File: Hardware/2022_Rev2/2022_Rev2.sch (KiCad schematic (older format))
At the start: 35 parts

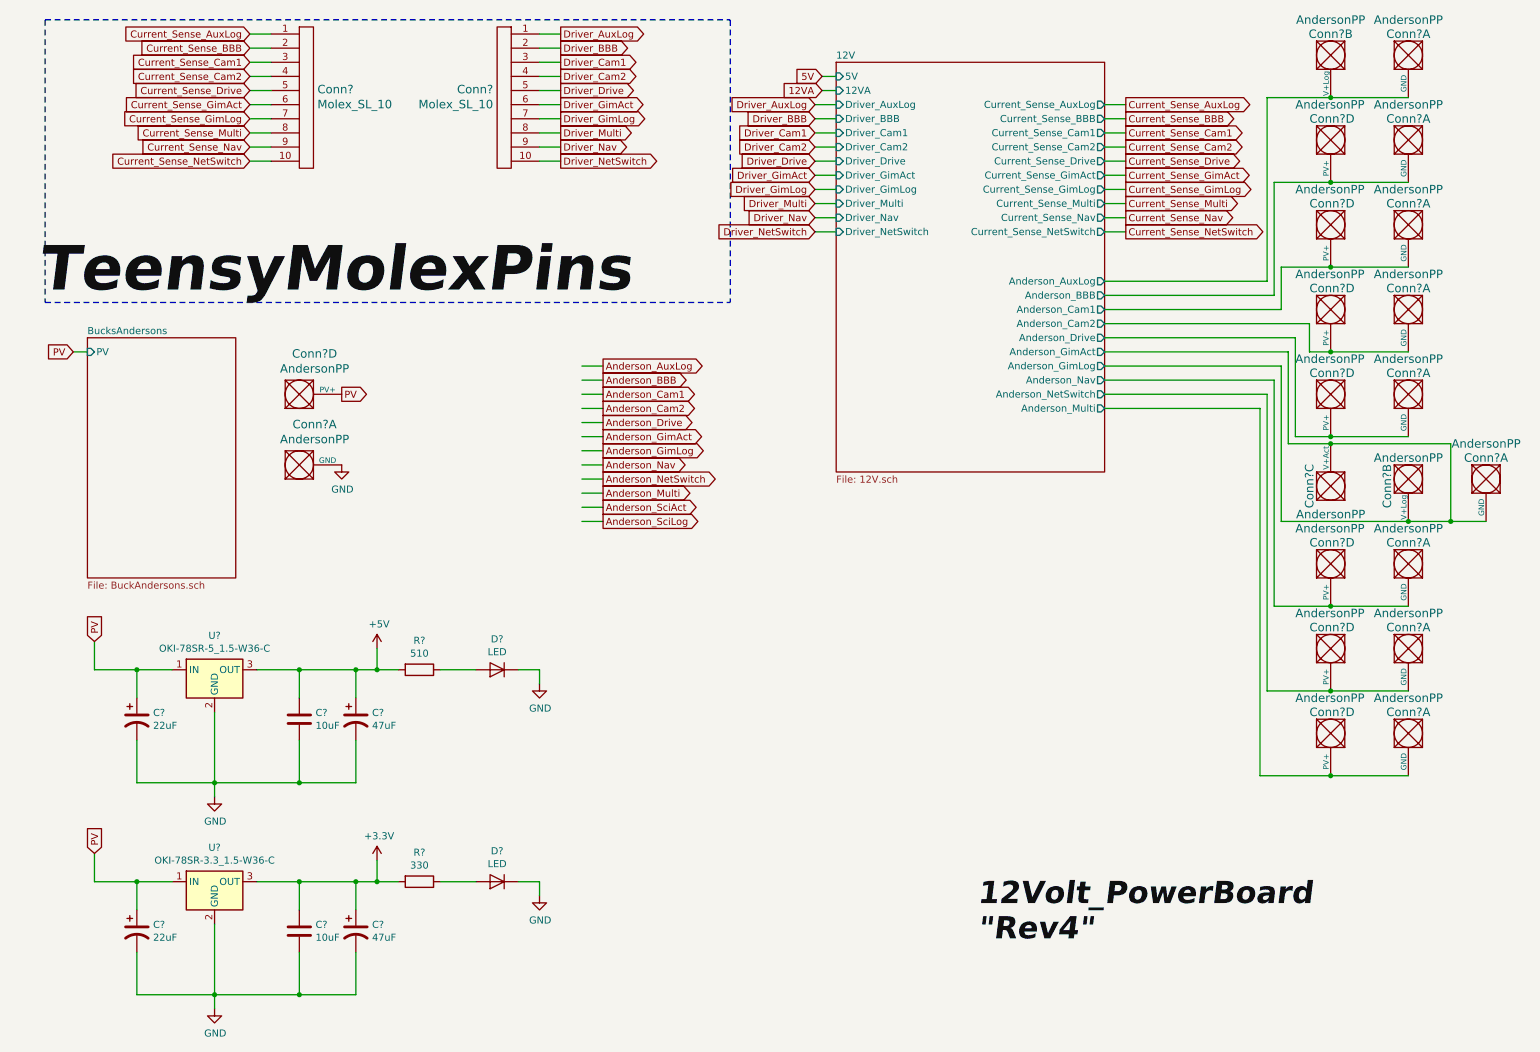
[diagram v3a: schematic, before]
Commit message: assigning footprints pt.1
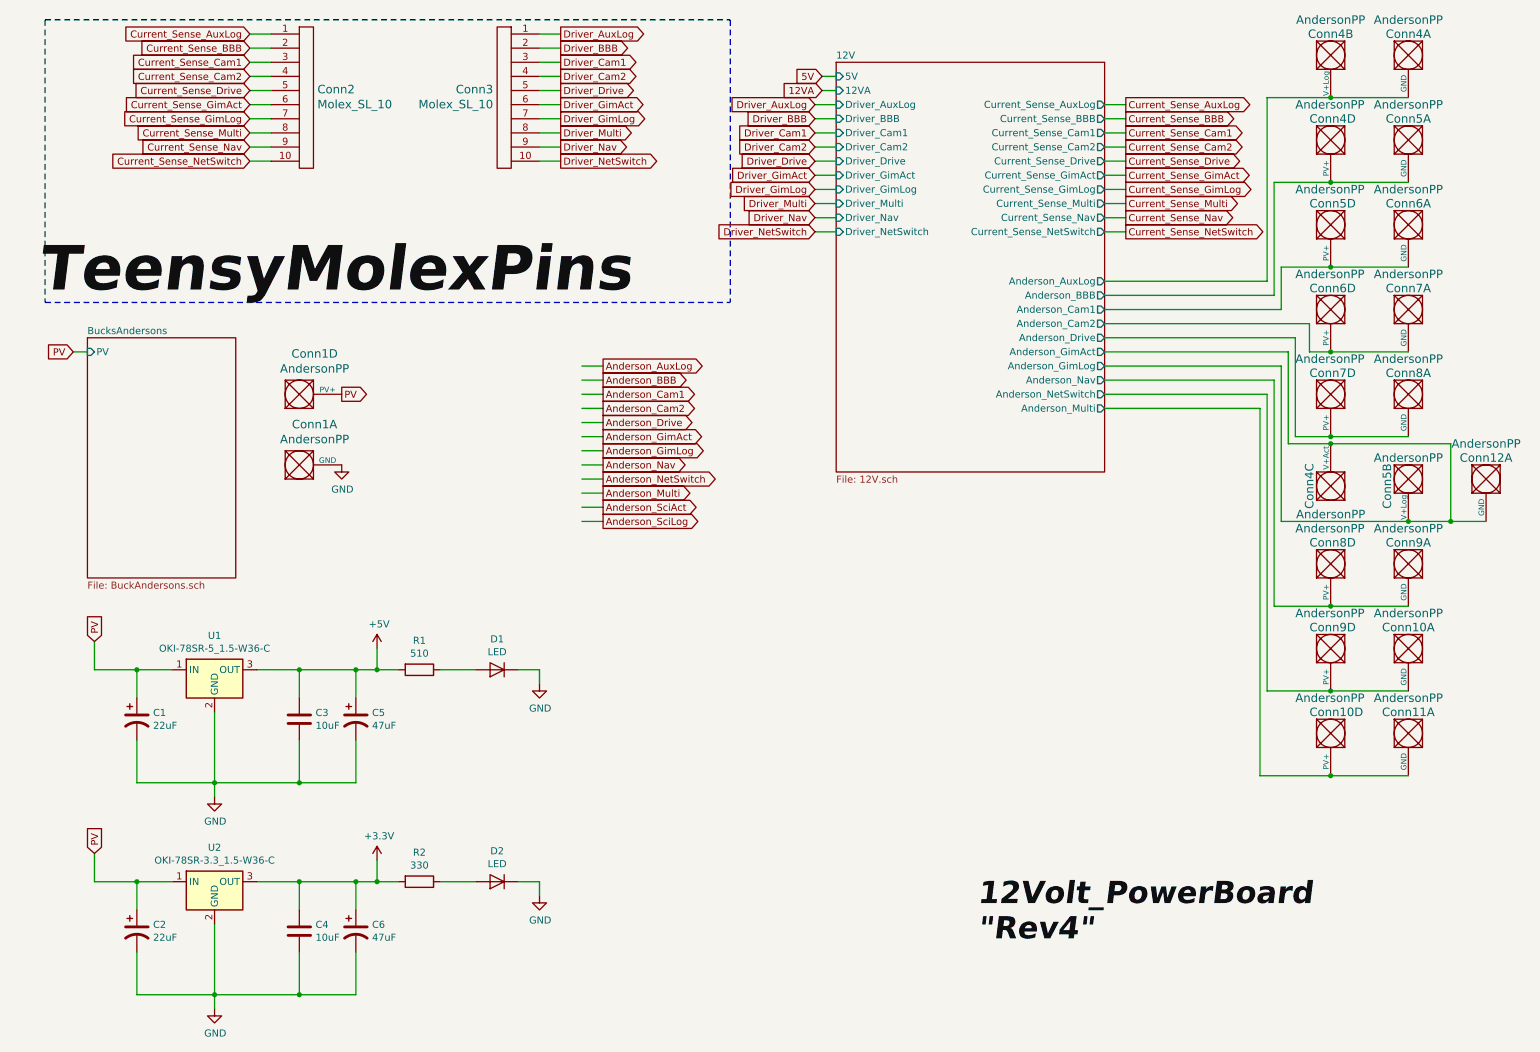
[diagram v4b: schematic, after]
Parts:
- C1, C2, C5, C6: renamed from C?; footprint (none) -> Capacitor_THT:CP_Radial_D6.3mm_P2.50mm
- C3, C4: renamed from C?; footprint (none) -> Capacitor_SMD:C_0603_1608Metric_Pad1.08x0.95mm_HandSolder
- D1, D2: renamed from D?; footprint (none) -> Diode_SMD:D_0603_1608Metric_Pad1.05x0.95mm_HandSolder
- gave numbers to parts that had none: 16

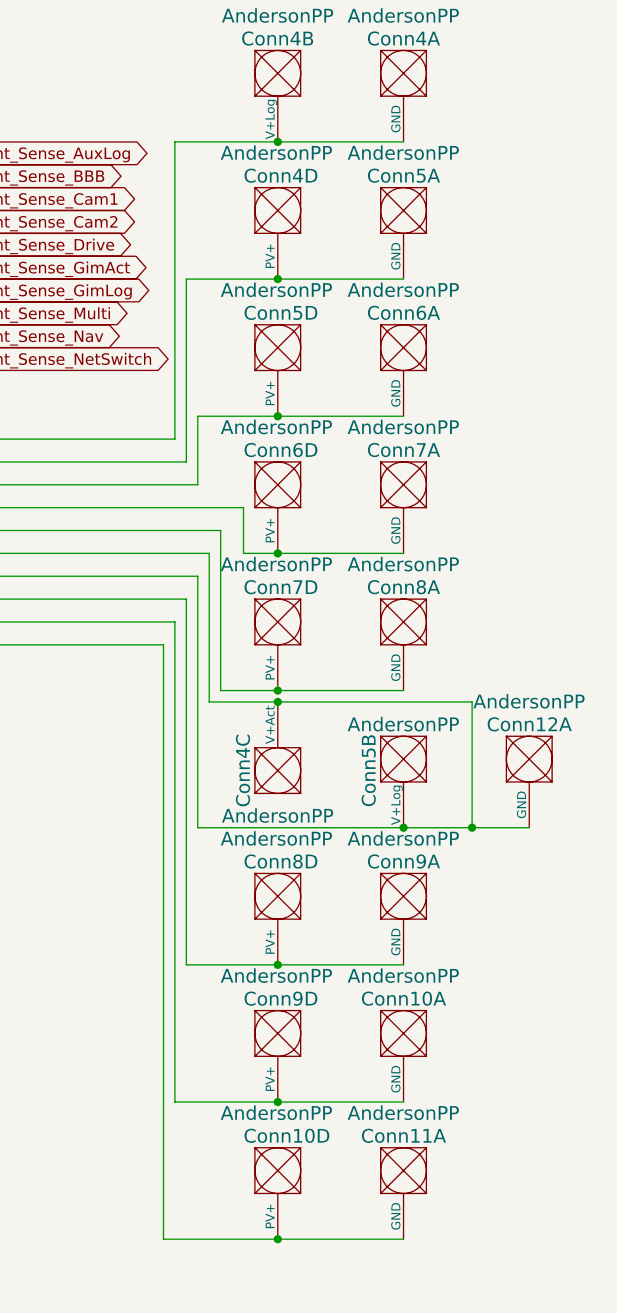
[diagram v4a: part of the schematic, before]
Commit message: Finished footprint signatures and started schematic
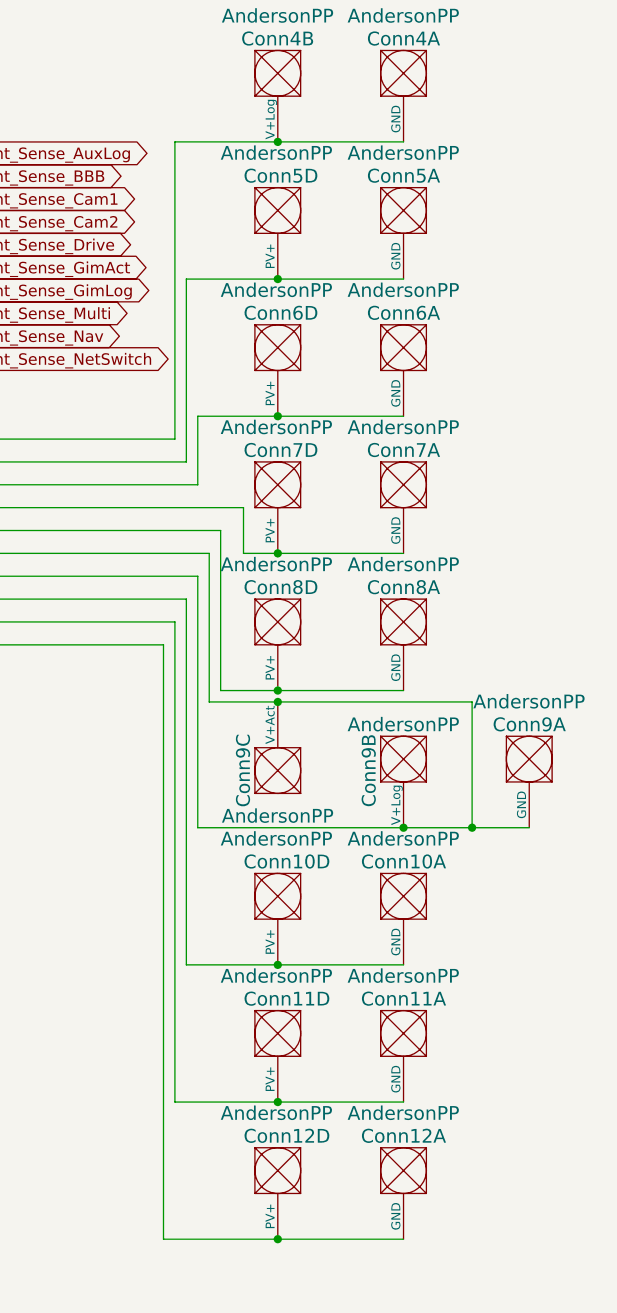
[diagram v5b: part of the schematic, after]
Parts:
- Conn1: footprint (none) -> MRDT_Connectors:Anderson_2_Vertical_Side_by_Side_PV
- Conn10, Conn11: renamed from Conn9; footprint (none) -> MRDT_Connectors:Anderson_2_Horizontal_Side_by_Side_PV
- Conn10: renamed from Conn8; footprint (none) -> MRDT_Connectors:Anderson_2_Horizontal_Side_by_Side_PV
- Conn11, Conn12: renamed from Conn10; footprint (none) -> MRDT_Connectors:Anderson_2_Horizontal_Side_by_Side_PV
- Conn12: renamed from Conn11; footprint (none) -> MRDT_Connectors:Anderson_2_Horizontal_Side_by_Side_PV
- Conn2, Conn3: footprint (none) -> MRDT_Connectors:MOLEX_SL_10_Vertical
- Conn4, Conn5, Conn6, Conn7, Conn8: footprint (none) -> MRDT_Connectors:Anderson_2_Horizontal_Side_by_Side_PV
- Conn5: renamed from Conn4; footprint (none) -> MRDT_Connectors:Anderson_2_Horizontal_Side_by_Side_PV
- Conn6: renamed from Conn5; footprint (none) -> MRDT_Connectors:Anderson_2_Horizontal_Side_by_Side_PV
- Conn7: renamed from Conn6; footprint (none) -> MRDT_Connectors:Anderson_2_Horizontal_Side_by_Side_PV
- Conn8: renamed from Conn7; footprint (none) -> MRDT_Connectors:Anderson_2_Horizontal_Side_by_Side_PV
- Conn9: renamed from Conn4; footprint (none) -> MRDT_Connectors:Anderson_3_Horizontal_Side_by_Side
- Conn9: renamed from Conn5; footprint (none) -> MRDT_Connectors:Anderson_3_Horizontal_Side_by_Side
- Conn9: renamed from Conn12; footprint (none) -> MRDT_Connectors:Anderson_3_Horizontal_Side_by_Side
- R1, R2: footprint (none) -> Resistor_SMD:R_0603_1608Metric_Pad0.98x0.95mm_HandSolder
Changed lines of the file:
@@
 F 0 "Conn1" H 2408 3637 60  0000 C CNN
 F 1 "AndersonPP" H 2408 3531 60  0000 C CNN
-F 2 "" H 2050 2700 60  0001 C CNN
+F 2 "MRDT_Connectors:Anderson_2_Vertical_Side_by_Side_PV" H 2050 2700 60  0001 C CNN
 F 3 "" H 2050 2700 60  0001 C CNN
 	4    2200 3250
@@
 F 0 "Conn1" H 2408 4137 60  0000 C CNN
 F 1 "AndersonPP" H 2408 4031 60  0000 C CNN
-F 2 "" H 2050 3200 60  0001 C CNN
+F 2 "MRDT_Connectors:Anderson_2_Vertical_Side_by_Side_PV" H 2050 3200 60  0001 C CNN
 F 3 "" H 2050 3200 60  0001 C CNN
 	1    2200 3750
@@
 F 0 "R1" V 2943 5100 50  0000 C CNN
 F 1 "510" V 3034 5100 50  0000 C CNN
-F 2 "" V 3080 5100 50  0001 C CNN
+F 2 "Resistor_SMD:R_0603_1608Metric_Pad0.98x0.95mm_HandSolder" V 3080 5100 50  0001 C CNN
 F 3 "~" H 3150 5100 50  0001 C CNN
 	1    3150 5100
@@
 F 0 "R2" V 2943 6600 50  0000 C CNN
 F 1 "330" V 3034 6600 50  0000 C CNN
-F 2 "" V 3080 6600 50  0001 C CNN
+F 2 "Resistor_SMD:R_0603_1608Metric_Pad0.98x0.95mm_HandSolder" V 3080 6600 50  0001 C CNN
 F 3 "~" H 3150 6600 50  0001 C CNN
 	1    3150 6600
@@
 F 0 "Conn4" V 9450 750 60  0000 C CNN
 F 1 "AndersonPP" V 9350 750 60  0000 C CNN
-F 2 "" H 9350 100 60  0001 C CNN
+F 2 "MRDT_Connectors:Anderson_2_Horizontal_Side_by_Side_PV" H 9350 100 60  0001 C CNN
 F 3 "" H 9350 100 60  0001 C CNN
 	2    9500 650
@@
 $EndComp
 $Comp
-L MRDT_Connectors:AndersonPP Conn12
+L MRDT_Connectors:AndersonPP Conn9
 U 1 1 62580F86
 P 10600 3650
-F 0 "Conn12" V 10550 3750 60  0000 C CNN
+F 0 "Conn9" V 10550 3750 60  0000 C CNN
 F 1 "AndersonPP" V 10450 3750 60  0000 C CNN
-F 2 "" H 10450 3100 60  0001 C CNN
+F 2 "MRDT_Connectors:Anderson_3_Horizontal_Side_by_Side" H 10450 3100 60  0001 C CNN
 F 3 "" H 10450 3100 60  0001 C CNN
 	1    10600 3650
@@
 F 0 "Conn4" V 10000 750 60  0000 C CNN
 F 1 "AndersonPP" V 9900 750 60  0000 C CNN
-F 2 "" H 9900 100 60  0001 C CNN
+F 2 "MRDT_Connectors:Anderson_2_Horizontal_Side_by_Side_PV" H 9900 100 60  0001 C CNN
 F 3 "" H 9900 100 60  0001 C CNN
 	1    10050 650
@@
 F 0 "Conn5" V 10000 1350 60  0000 C CNN
 F 1 "AndersonPP" V 9900 1350 60  0000 C CNN
-F 2 "" H 9900 700 60  0001 C CNN
+F 2 "MRDT_Connectors:Anderson_2_Horizontal_Side_by_Side_PV" H 9900 700 60  0001 C CNN
 F 3 "" H 9900 700 60  0001 C CNN
 	1    10050 1250
@@
 F 0 "Conn6" V 10000 1950 60  0000 C CNN
 F 1 "AndersonPP" V 9900 1950 60  0000 C CNN
-F 2 "" H 9900 1300 60  0001 C CNN
+F 2 "MRDT_Connectors:Anderson_2_Horizontal_Side_by_Side_PV" H 9900 1300 60  0001 C CNN
 F 3 "" H 9900 1300 60  0001 C CNN
 	1    10050 1850
@@
 F 0 "Conn7" V 10000 2550 60  0000 C CNN
 F 1 "AndersonPP" V 9900 2550 60  0000 C CNN
-F 2 "" H 9900 1900 60  0001 C CNN
+F 2 "MRDT_Connectors:Anderson_2_Horizontal_Side_by_Side_PV" H 9900 1900 60  0001 C CNN
 F 3 "" H 9900 1900 60  0001 C CNN
 	1    10050 2450
@@
 $EndComp
 $Comp
-L MRDT_Connectors:AndersonPP Conn4
+L MRDT_Connectors:AndersonPP Conn9
 U 3 1 6257FC90
 P 9700 3900
-F 0 "Conn4" H 9800 4150 60  0000 C CNN
+F 0 "Conn9" H 9800 4150 60  0000 C CNN
 F 1 "AndersonPP" V 9600 4000 60  0000 C CNN
-F 2 "" H 9550 3350 60  0001 C CNN
+F 2 "MRDT_Connectors:Anderson_3_Horizontal_Side_by_Side" H 9550 3350 60  0001 C CNN
 F 3 "" H 9550 3350 60  0001 C CNN
 	3    9700 3900
@@
 $EndComp
 $Comp
-L MRDT_Connectors:AndersonPP Conn9
+L MRDT_Connectors:AndersonPP Conn10
 U 1 1 625DF808
 P 10050 4250
-F 0 "Conn9" V 10000 4350 60  0000 C CNN
+F 0 "Conn10" V 10000 4350 60  0000 C CNN
 F 1 "AndersonPP" V 9900 4350 60  0000 C CNN
-F 2 "" H 9900 3700 60  0001 C CNN
+F 2 "MRDT_Connectors:Anderson_2_Horizontal_Side_by_Side_PV" H 9900 3700 60  0001 C CNN
 F 3 "" H 9900 3700 60  0001 C CNN
 	1    10050 4250
@@
 $EndComp
 $Comp
-L MRDT_Connectors:AndersonPP Conn10
+L MRDT_Connectors:AndersonPP Conn11
 U 1 1 625E3A96
 P 10050 4850
-F 0 "Conn10" V 10000 4950 60  0000 C CNN
+F 0 "Conn11" V 10000 4950 60  0000 C CNN
 F 1 "AndersonPP" V 9900 4950 60  0000 C CNN
-F 2 "" H 9900 4300 60  0001 C CNN
+F 2 "MRDT_Connectors:Anderson_2_Horizontal_Side_by_Side_PV" H 9900 4300 60  0001 C CNN
 F 3 "" H 9900 4300 60  0001 C CNN
 	1    10050 4850
@@
 $EndComp
 $Comp
-L MRDT_Connectors:AndersonPP Conn11
+L MRDT_Connectors:AndersonPP Conn12
 U 1 1 625EBE27
 P 10050 5450
-F 0 "Conn11" V 10000 5550 60  0000 C CNN
+F 0 "Conn12" V 10000 5550 60  0000 C CNN
 F 1 "AndersonPP" V 9900 5550 60  0000 C CNN
-F 2 "" H 9900 4900 60  0001 C CNN
+F 2 "MRDT_Connectors:Anderson_2_Horizontal_Side_by_Side_PV" H 9900 4900 60  0001 C CNN
 F 3 "" H 9900 4900 60  0001 C CNN
 	1    10050 5450
@@
 	9450 2650 9450 2850
 $Comp
-L MRDT_Connectors:AndersonPP Conn4
+L MRDT_Connectors:AndersonPP Conn5
 U 4 1 6265DE23
 P 9500 1250
-F 0 "Conn4" V 9450 1200 60  0000 L CNN
+F 0 "Conn5" V 9450 1200 60  0000 L CNN
 F 1 "AndersonPP" V 9350 1100 60  0000 L CNN
-F 2 "" H 9350 700 60  0001 C CNN
+F 2 "MRDT_Connectors:Anderson_2_Horizontal_Side_by_Side_PV" H 9350 700 60  0001 C CNN
 F 3 "" H 9350 700 60  0001 C CNN
 	4    9500 1250
@@
 	9600 1650 10150 1650
 $Comp
-L MRDT_Connectors:AndersonPP Conn5
+L MRDT_Connectors:AndersonPP Conn6
 U 4 1 62664C16
 P 9500 1850
-F 0 "Conn5" V 9450 1800 60  0000 L CNN
+F 0 "Conn6" V 9450 1800 60  0000 L CNN
 F 1 "AndersonPP" V 9350 1700 60  0000 L CNN
-F 2 "" H 9350 1300 60  0001 C CNN
+F 2 "MRDT_Connectors:Anderson_2_Horizontal_Side_by_Side_PV" H 9350 1300 60  0001 C CNN
 F 3 "" H 9350 1300 60  0001 C CNN
 	4    9500 1850
@@
 $EndComp
 $Comp
-L MRDT_Connectors:AndersonPP Conn6
+L MRDT_Connectors:AndersonPP Conn7
 U 4 1 62669E3D
 P 9500 2450
-F 0 "Conn6" V 9450 2400 60  0000 L CNN
+F 0 "Conn7" V 9450 2400 60  0000 L CNN
 F 1 "AndersonPP" V 9350 2300 60  0000 L CNN
-F 2 "" H 9350 1900 60  0001 C CNN
+F 2 "MRDT_Connectors:Anderson_2_Horizontal_Side_by_Side_PV" H 9350 1900 60  0001 C CNN
 F 3 "" H 9350 1900 60  0001 C CNN
 	4    9500 2450
@@
 $EndComp
 $Comp
-L MRDT_Connectors:AndersonPP Conn7
+L MRDT_Connectors:AndersonPP Conn8
 U 4 1 62679AA7
 P 9500 3050
-F 0 "Conn7" V 9450 3000 60  0000 L CNN
+F 0 "Conn8" V 9450 3000 60  0000 L CNN
 F 1 "AndersonPP" V 9350 2900 60  0000 L CNN
-F 2 "" H 9350 2500 60  0001 C CNN
+F 2 "MRDT_Connectors:Anderson_2_Horizontal_Side_by_Side_PV" H 9350 2500 60  0001 C CNN
 F 3 "" H 9350 2500 60  0001 C CNN
 	4    9500 3050
@@
 F 0 "Conn8" V 10000 3150 60  0000 C CNN
 F 1 "AndersonPP" V 9900 3150 60  0000 C CNN
-F 2 "" H 9900 2500 60  0001 C CNN
+F 2 "MRDT_Connectors:Anderson_2_Horizontal_Side_by_Side_PV" H 9900 2500 60  0001 C CNN
 F 3 "" H 9900 2500 60  0001 C CNN
 	1    10050 3050
@@
 	9600 2250 10150 2250
 $Comp
-L MRDT_Connectors:AndersonPP Conn8
+L MRDT_Connectors:AndersonPP Conn10
 U 4 1 62690D22
 P 9500 4250
-F 0 "Conn8" V 9450 4200 60  0000 L CNN
+F 0 "Conn10" V 9450 4200 60  0000 L CNN
 F 1 "AndersonPP" V 9350 4100 60  0000 L CNN
-F 2 "" H 9350 3700 60  0001 C CNN
+F 2 "MRDT_Connectors:Anderson_2_Horizontal_Side_by_Side_PV" H 9350 3700 60  0001 C CNN
 F 3 "" H 9350 3700 60  0001 C CNN
 	4    9500 4250
@@
 $EndComp
 $Comp
-L MRDT_Connectors:AndersonPP Conn9
+L MRDT_Connectors:AndersonPP Conn11
 U 4 1 626957E9
 P 9500 4850
-F 0 "Conn9" V 9450 4800 60  0000 L CNN
+F 0 "Conn11" V 9450 4800 60  0000 L CNN
 F 1 "AndersonPP" V 9350 4700 60  0000 L CNN
-F 2 "" H 9350 4300 60  0001 C CNN
+F 2 "MRDT_Connectors:Anderson_2_Horizontal_Side_by_Side_PV" H 9350 4300 60  0001 C CNN
 F 3 "" H 9350 4300 60  0001 C CNN
 	4    9500 4850
@@
 $EndComp
 $Comp
-L MRDT_Connectors:AndersonPP Conn10
+L MRDT_Connectors:AndersonPP Conn12
 U 4 1 6269A40C
 P 9500 5450
-F 0 "Conn10" V 9450 5400 60  0000 L CNN
+F 0 "Conn12" V 9450 5400 60  0000 L CNN
 F 1 "AndersonPP" V 9350 5300 60  0000 L CNN
-F 2 "" H 9350 4900 60  0001 C CNN
+F 2 "MRDT_Connectors:Anderson_2_Horizontal_Side_by_Side_PV" H 9350 4900 60  0001 C CNN
 F 3 "" H 9350 4900 60  0001 C CNN
 	4    9500 5450
@@
 	9350 2750 9350 3450
 $Comp
-L MRDT_Connectors:AndersonPP Conn5
+L MRDT_Connectors:AndersonPP Conn9
 U 2 1 62580207
 P 10050 3650
-F 0 "Conn5" H 10200 3600 60  0000 C CNN
+F 0 "Conn9" H 10200 3600 60  0000 C CNN
 F 1 "AndersonPP" V 10000 3750 60  0000 C CNN
-F 2 "" H 9900 3100 60  0001 C CNN
+F 2 "MRDT_Connectors:Anderson_3_Horizontal_Side_by_Side" H 9900 3100 60  0001 C CNN
 F 3 "" H 9900 3100 60  0001 C CNN
 	2    10050 3650
@@
 F 0 "Conn2" H 2428 2108 60  0000 L CNN
 F 1 "Molex_SL_10" H 2428 2002 60  0000 L CNN
-F 2 "" H 2300 2050 60  0001 C CNN
+F 2 "MRDT_Connectors:MOLEX_SL_10_Vertical" H 2300 2050 60  0001 C CNN
 F 3 "" H 2300 2050 60  0001 C CNN
 	1    2300 1550
@@
 F 0 "Conn3" H 3928 2108 60  0000 L CNN
 F 1 "Molex_SL_10" H 3928 2002 60  0000 L CNN
-F 2 "" H 3800 2050 60  0001 C CNN
+F 2 "MRDT_Connectors:MOLEX_SL_10_Vertical" H 3800 2050 60  0001 C CNN
 F 3 "" H 3800 2050 60  0001 C CNN
 	1    3800 1550
